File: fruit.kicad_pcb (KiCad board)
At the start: 2 copper layers, 161.6 x 100 mm, 3 parts

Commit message: respin
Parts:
- removed MK2 (x2): Mounting_Hole_PAD, Mounting_Holes:MountingHole_2.7mm
- removed REF**: BUS_PCIexpress_x4, Connector_PCIe_MyOwn:BUS_PCIexpress_x4_Salmonberry_reduced_shoulders
- added C1: 10uF, Capacitor_SMD:C_0402_1005Metric, F.Cu at (548.5, 31.0)
- added C10: 10uF, Capacitor_SMD:C_0402_1005Metric, F.Cu at (475.4, 112.2)
- added C11: 0.1uF, Capacitor_SMD:C_0402_1005Metric, F.Cu at (484.5, 102.6)
- added C12: 1uF, Capacitor_SMD:C_0402_1005Metric, F.Cu at (335.8, 127.8)
- added C13: 1uF, Capacitor_SMD:C_0402_1005Metric, F.Cu at (347.8, 118.3)
- added C14: 0.1uF, Capacitor_SMD:C_0402_1005Metric, F.Cu at (344.9, 120.2)
- added C15: 1uF, Capacitor_SMD:C_0402_1005Metric, F.Cu at (335.8, 129.8)
- added C16: 470pF, Capacitor_SMD:C_0402_1005Metric, F.Cu at (347.7, 120.2)
- added C17: 470pF, Capacitor_SMD:C_0402_1005Metric, F.Cu at (338.8, 125.8)
- added C18: 1uF, Capacitor_SMD:C_0402_1005Metric, F.Cu at (329.2, 139.6)
- added C19: 0.1uF, Capacitor_SMD:C_0402_1005Metric, F.Cu at (341.7, 123.8)
- added C2: 0.1uF, Capacitor_SMD:C_0402_1005Metric, F.Cu at (557.6, 21.4)
- added C20: 0.1uF, Capacitor_SMD:C_0805_2012Metric, F.Cu at (513.1, -59.4)
- added C21: 0.1uF, Capacitor_SMD:C_0805_2012Metric, F.Cu at (496.2, -36.9)
- added C22: 0.1uF, Capacitor_SMD:C_0402_1005Metric, F.Cu at (483.8, 41.3)
- added C23: 1uF, Capacitor_SMD:C_0402_1005Metric, F.Cu at (489.4, 35.3)
- added C24: 0.1uF, Capacitor_SMD:C_0402_1005Metric, F.Cu at (478.3, 46.9)
- added C25: 0.1uF, Capacitor_SMD:C_0402_1005Metric, F.Cu at (496.7, 28.6)
- added C26: 10uF, Capacitor_SMD:C_0805_2012Metric, F.Cu at (495.8, 21.9)
- added C27: 100uF, Capacitor_SMD:C_1210_3225Metric, F.Cu at (490.7, 22.5)
- added C28: 10uF, Capacitor_SMD:C_0805_2012Metric, F.Cu at (476.2, 41.8)
- added C29: 10uF, Capacitor_SMD:C_0805_2012Metric, F.Cu at (490.1, 26.1)
- added C3: 10uF, Capacitor_SMD:C_0402_1005Metric, F.Cu at (335.9, 37.0)
- added C30: 10uF, Capacitor_SMD:C_0805_2012Metric, F.Cu at (490.1, 29.1)
- added C31: 10uF, Capacitor_SMD:C_0805_2012Metric, F.Cu at (494.6, 26.1)
- added C32: 10uF 35V, Capacitor_SMD:C_1206_3216Metric, F.Cu at (575.5, -46.9)
- added C33: 10uF 35V, Capacitor_SMD:C_1206_3216Metric, F.Cu at (569.9, -40.2)
- added C34: 10uF 35V, Capacitor_SMD:C_1206_3216Metric, F.Cu at (569.9, -43.5)
- added C35: 10uF 35V, Capacitor_SMD:C_1206_3216Metric, F.Cu at (569.9, -46.9)
- added C36: 10uF 35V, Capacitor_SMD:C_1206_3216Metric, F.Cu at (587.8, -59.2)
- added C37: 10uF 35V, Capacitor_SMD:C_1206_3216Metric, F.Cu at (578.6, -51.6)
- added C38: 0.1uF, Capacitor_SMD:C_0402_1005Metric, F.Cu at (596.5, -59.9)
- added C39: 0.1uF, Capacitor_SMD:C_0402_1005Metric, F.Cu at (571.4, -35.0)
- added C4: 0.1uF, Capacitor_SMD:C_0402_1005Metric, F.Cu at (329.2, 45.2)
- added C40: DNP, Capacitor_SMD:C_0402_1005Metric, F.Cu at (590.9, -54.5)
- added C41: 1.2nF, Capacitor_SMD:C_0402_1005Metric, F.Cu at (572.5, -37.5)
- added C43: 10uF, Capacitor_SMD:C_0805_2012Metric, F.Cu at (587.2, -56.0)
- added C44: 10uF, Capacitor_SMD:C_0805_2012Metric, F.Cu at (574.9, -43.7)
- added C45: 10uF, Capacitor_SMD:C_0805_2012Metric, F.Cu at (592.8, -59.4)
- added C46: 10uF, Capacitor_SMD:C_0805_2012Metric, F.Cu at (583.6, -51.8)
- added C47: 100uF, Capacitor_Tantalum_SMD_MyOwn:CP_EIA-7343-31_Kemet-D, F.Cu at (572.0, -58.0)
- added C48: 10uF 35V, Capacitor_SMD:C_1206_3216Metric, F.Cu at (421.6, 103.3)
- added C49: 10uF 35V, Capacitor_SMD:C_1206_3216Metric, F.Cu at (409.3, 115.6)
- added C5: 10uF, Capacitor_SMD:C_0402_1005Metric, F.Cu at (360.2, -53.3)
- added C50: 10uF 35V, Capacitor_SMD:C_1206_3216Metric, F.Cu at (412.4, 110.8)
- added C51: 10uF 35V, Capacitor_SMD:C_1206_3216Metric, F.Cu at (403.7, 119.0)
- added C52: 10uF 35V, Capacitor_SMD:C_1206_3216Metric, F.Cu at (403.7, 115.6)
- added C53: 10uF 35V, Capacitor_SMD:C_1206_3216Metric, F.Cu at (403.7, 122.3)
- added C54: 0.1uF, Capacitor_SMD:C_0402_1005Metric, F.Cu at (430.3, 102.6)
- added C55: 0.1uF, Capacitor_SMD:C_0402_1005Metric, F.Cu at (406.4, 125.0)
- added C56: DNP, Capacitor_SMD:C_0402_1005Metric, F.Cu at (405.2, 127.5)
- added C57: 1.2nF, Capacitor_SMD:C_0402_1005Metric, F.Cu at (424.6, 108.0)
- added C59: 10uF, Capacitor_SMD:C_0805_2012Metric, F.Cu at (408.7, 118.8)
- added C6: 0.1uF, Capacitor_SMD:C_0402_1005Metric, F.Cu at (349.2, -42.5)
- added C60: 10uF, Capacitor_SMD:C_0805_2012Metric, F.Cu at (417.4, 110.7)
- added C61: 10uF, Capacitor_SMD:C_0805_2012Metric, F.Cu at (421.0, 106.5)
- added C62: 10uF, Capacitor_SMD:C_0805_2012Metric, F.Cu at (426.6, 103.1)
- added C63: 100uF, Capacitor_Tantalum_SMD_MyOwn:CP_EIA-7343-31_Kemet-D, F.Cu at (405.8, 104.5)
- added C64: 10uF, Capacitor_SMD:C_0402_1005Metric, F.Cu at (41.9, -30.5)
- added C65: 10uF, Capacitor_SMD:C_0402_1005Metric, F.Cu at (124.9, -54.0)
- added C66: 10uF, Capacitor_SMD:C_0402_1005Metric, F.Cu at (47.6, -32.5)
- added C67: 1uF, Capacitor_SMD:C_0402_1005Metric, F.Cu at (36.0, -26.5)
- added C68: 1uF, Capacitor_SMD:C_0402_1005Metric, F.Cu at (33.1, -24.5)
- added C69: 10nF, Capacitor_SMD:C_0402_1005Metric, F.Cu at (39.0, -28.5)
- added C7: 10uF, Capacitor_SMD:C_0805_2012Metric, F.Cu at (445.2, -59.4)
- added C70: 10nF, Capacitor_SMD:C_0402_1005Metric, F.Cu at (33.1, -22.6)
- added C71: 10nF, Capacitor_SMD:C_0402_1005Metric, F.Cu at (36.0, -24.5)
- added C72: 10nF, Capacitor_SMD:C_0402_1005Metric, F.Cu at (36.0, -22.6)
- added C73: 10nF, Capacitor_SMD:C_0402_1005Metric, F.Cu at (44.8, -32.5)
- added C74: 0.1uF, Capacitor_SMD:C_0402_1005Metric, F.Cu at (38.9, -24.6)
- added C8: 10uF, Capacitor_SMD:C_0805_2012Metric, F.Cu at (423.1, -35.6)
- added C9: 10uF, Capacitor_SMD:C_0805_2012Metric, F.Cu at (440.7, -59.4)
- added CM1: ComputeModule4-CM4, Connector_RaspberryPi:Raspberry-Pi-4-Compute-Module_outline, F.Cu at (221.8, -33.1)
- added COOLER1: 53-61mm_NorthBridge_45deg_arms, Mechanical_CoolingBlock:53-61mm_NorthBridge_45deg_arms, F.Cu at (254.9, 103.0)
- added D1: LED Red, LED_SMD_LiteOn:LED_0603_1608Metric_red, F.Cu at (353.9, -53.4)
- added D2: LED Green, LED_SMD_LiteOn:LED_0603_1608Metric_green, F.Cu at (349.8, -50.8)
- added D3: LED Yellow, LED_SMD_LiteOn:LED_0603_1608Metric_yellow, F.Cu at (356.5, -57.0)
- added D4: LED Green, LED_SMD_LiteOn:LED_0603_1608Metric_green, F.Cu at (360.5, -59.6)
- added D5: LED Orange, LED_SMD_LiteOn:LED_0603_1608Metric_orange, F.Cu at (349.8, -53.4)
- added D6: LED Blue, LED_SMD_LiteOn:LED_0603_1608Metric_blue, F.Cu at (356.5, -59.6)
- added D7: LED Green, LED_SMD_LiteOn:LED_0603_1608Metric_green, F.Cu at (476.0, 44.6)
- added D8: LED Green, LED_SMD_LiteOn:LED_0603_1608Metric_green, F.Cu at (569.1, -37.3)
- added D9: LED Green, LED_SMD_LiteOn:LED_0603_1608Metric_green, F.Cu at (402.9, 125.2)
- added FID1: Fiducial, Fiducial:Fiducial_1mm_Mask2mm, F.Cu at (306.1, -59.1)
- added FID2: Fiducial, Fiducial:Fiducial_1mm_Mask2mm, F.Cu at (292.2, -52.1)
- added FID3: Fiducial, Fiducial:Fiducial_1mm_Mask2mm, F.Cu at (221.1, 30.6)
- added H1: MountingHole, MountingHole:MountingHole_2.7mm_M2.5, F.Cu at (3.57, 5.55)
- added H2: MountingHole, MountingHole:MountingHole_2.7mm_M2.5, F.Cu at (3.57, 94.5)
- added J1: PCB_Edge_PCI_Express_x4_Salmonberry, Connector_PCIe_MyOwn:BUS_PCIexpress_x4_Salmonberry_reduced_shoulders, B.Cu at (163.6, 33.5)
- added J2: 2086581051, Connector_HDMI_Molex:2086581051, F.Cu at (429.7, -52.4)
- added J3: TSM-102-01-L-SV, Connector_Header_Samtec:SAMTEC_TSM-102-01-L-SV, F.Cu at (331.1, 121.2)
- added J4: TSM-102-01-L-SV, Connector_Header_Samtec:SAMTEC_TSM-102-01-L-SV, F.Cu at (331.1, 129.1)
- added J5: MEM2067-02-180-00-A_REVB, Connector_SD_GCT:GCT_MEM2067-02-180-00-A_REVB, F.Cu at (502.4, -52.9)
- added J6: USB4110-GF-A, Connector_USB_GCT:USB4110-GF-A, F.Cu at (480.9, 23.3)
- added J7: USB4110-GF-A, Connector_USB_GCT:USB4110-GF-A, F.Cu at (480.9, 33.3)
- added J8: 1-2199119-6, Connector_M.2_TE:1-2199119-6_2280_standoff_nooutline, F.Cu at (115.0, -45.0)
- added L1: SRN6045TA-3R3Y, Inductor_SMD:L_Bourns_SRN6045TA, F.Cu at (580.9, -57.1)
- added L2: SRN6045TA-3R3Y, Inductor_SMD:L_Bourns_SRN6045TA, F.Cu at (414.7, 105.4)
- added R1: 5.1k, Resistor_SMD:R_0402_1005Metric, F.Cu at (329.2, 43.3)
- added R10: 1k, Resistor_SMD:R_0402_1005Metric, F.Cu at (357.3, -54.7)
- added R11: 1k, Resistor_SMD:R_0402_1005Metric, F.Cu at (355.0, -49.0)
- added R12: 1k, Resistor_SMD:R_0402_1005Metric, F.Cu at (349.2, -46.5)
- added R13: 1k, Resistor_SMD:R_0402_1005Metric, F.Cu at (353.3, -51.0)
- added R14: 1k, Resistor_SMD:R_0402_1005Metric, F.Cu at (364.0, -59.9)
- added R15: 1k, Resistor_SMD:R_0402_1005Metric, F.Cu at (356.2, -51.0)
- added R16: 10k, Resistor_SMD:R_0402_1005Metric, F.Cu at (422.3, -33.1)
- added R17: 15k 1%, Resistor_SMD:R_0402_1005Metric, F.Cu at (427.4, -44.6)
- added R18: 1k, Resistor_SMD:R_0402_1005Metric, F.Cu at (329.2, 137.6)
- added R19: 1k, Resistor_SMD:R_0402_1005Metric, F.Cu at (344.9, 118.3)
- added R2: 1k, Resistor_SMD:R_0402_1005Metric, F.Cu at (349.2, -44.5)
- added R20: 1k, Resistor_SMD:R_0402_1005Metric, F.Cu at (335.9, 121.8)
- added R21: 1k, Resistor_SMD:R_0402_1005Metric, F.Cu at (335.9, 123.8)
- added R22: 1k, Resistor_SMD:R_0402_1005Metric, F.Cu at (341.7, 121.9)
- added R23: 1k, Resistor_SMD:R_0402_1005Metric, F.Cu at (338.8, 121.9)
- added R24: 1k, Resistor_SMD:R_0402_1005Metric, F.Cu at (335.9, 125.8)
- added R25: 1k, Resistor_SMD:R_0402_1005Metric, F.Cu at (334.7, 134.1)
- added R26: 1k, Resistor_SMD:R_0402_1005Metric, F.Cu at (338.8, 123.9)
- added R27: 12k 1%, Resistor_SMD:R_0402_1005Metric, F.Cu at (516.8, -59.9)
- added R28: 330R, Resistor_SMD:R_0402_1005Metric, F.Cu at (502.4, 21.4)
- added R29: 5.1k, Resistor_SMD:R_0402_1005Metric, F.Cu at (498.3, 24.4)
- added R3: 1k, Resistor_SMD:R_0402_1005Metric, F.Cu at (359.9, -57.3)
- added R30: 2.2K 1%, Resistor_SMD:R_0402_1005Metric, F.Cu at (498.3, 26.4)
- added R31: 2.2K 1%, Resistor_SMD:R_0402_1005Metric, F.Cu at (475.4, 48.9)
- added R32: 330R, Resistor_SMD:R_0402_1005Metric, F.Cu at (493.8, 28.6)
- added R33: 330R, Resistor_SMD:R_0402_1005Metric, F.Cu at (493.8, 30.6)
- added R34: 5.1k, Resistor_SMD:R_0402_1005Metric, F.Cu at (499.5, 21.4)
- added R35: 10k, Resistor_SMD:R_0402_1005Metric, F.Cu at (479.5, 44.8)
- added R36: 15k 1%, Resistor_SMD:R_0402_1005Metric, F.Cu at (475.4, 46.9)
- added R37: 10R, Resistor_SMD:R_0402_1005Metric, F.Cu at (579.8, -45.9)
- added R38: 12k 1%, Resistor_SMD:R_0402_1005Metric, F.Cu at (587.3, -53.5)
- added R39: 47k 1%, Resistor_SMD:R_0402_1005Metric, F.Cu at (590.9, -56.5)
- added R4: 1k, Resistor_SMD:R_0402_1005Metric, F.Cu at (349.2, -48.5)
- added R40: 15k 1%, Resistor_SMD:R_0402_1005Metric, F.Cu at (568.5, -34.9)
- added R41: 1k, Resistor_SMD:R_0402_1005Metric, F.Cu at (582.9, -49.3)
- added R42: 10R, Resistor_SMD:R_0402_1005Metric, F.Cu at (421.1, 109.0)
- added R43: 20k 1%, Resistor_SMD:R_0402_1005Metric, F.Cu at (416.7, 113.2)
- added R44: 12k 1%, Resistor_SMD:R_0402_1005Metric, F.Cu at (402.3, 127.6)
- added R45: 2.2K 1%, Resistor_SMD:R_0402_1005Metric, F.Cu at (424.7, 106.0)
- added R46: 1k, Resistor_SMD:R_0402_1005Metric, F.Cu at (413.6, 116.6)
- added R47: 50R, Resistor_SMD:R_0402_1005Metric, F.Cu at (122.0, -52.0)
- added R48: 50R, Resistor_SMD:R_0402_1005Metric, F.Cu at (122.0, -53.9)
- added R49: 50R, Resistor_SMD:R_0402_1005Metric, F.Cu at (39.0, -30.5)
- added R5: 5.1k, Resistor_SMD:R_0402_1005Metric, F.Cu at (352.1, -46.5)
- added R50: 50R, Resistor_SMD:R_0402_1005Metric, F.Cu at (36.1, -30.5)
- added R51: 50R, Resistor_SMD:R_0402_1005Metric, F.Cu at (41.9, -32.5)
- added R52: 50R, Resistor_SMD:R_0402_1005Metric, F.Cu at (39.0, -32.5)
- added R53: 50R, Resistor_SMD:R_0402_1005Metric, F.Cu at (36.1, -28.5)
- added R54: 50R, Resistor_SMD:R_0402_1005Metric, F.Cu at (33.2, -32.5)
- added R55: 50R, Resistor_SMD:R_0402_1005Metric, F.Cu at (33.2, -26.5)
- added R56: 50R, Resistor_SMD:R_0402_1005Metric, F.Cu at (36.1, -32.5)
- added R57: 50R, Resistor_SMD:R_0402_1005Metric, F.Cu at (33.2, -28.5)
- added R58: 50R, Resistor_SMD:R_0402_1005Metric, F.Cu at (122.0, -55.9)
- added R59: 50R, Resistor_SMD:R_0402_1005Metric, F.Cu at (125.0, -55.9)
- added R6: 5.1k, Resistor_SMD:R_0402_1005Metric, F.Cu at (362.9, -57.3)
- added R60: 50R, Resistor_SMD:R_0402_1005Metric, F.Cu at (33.2, -30.5)
- added R7: 1k, Resistor_SMD:R_0402_1005Metric, F.Cu at (360.2, -55.3)
- added R8: 1k, Resistor_SMD:R_0402_1005Metric, F.Cu at (352.1, -48.5)
- added R9: 1k, Resistor_SMD:R_0402_1005Metric, F.Cu at (366.9, -59.9)
- added TP1: TestPoint, TestPoint:TestPoint_Pad_D1.0mm, F.Cu at (548.6, 28.5)
- added TP2: TestPoint, TestPoint:TestPoint_Pad_D1.0mm, F.Cu at (475.5, 109.7)
- added TP3: TestPoint, TestPoint:TestPoint_Pad_D1.0mm, F.Cu at (579.9, -48.5)
- added TP4: TestPoint, TestPoint:TestPoint_Pad_D1.0mm, F.Cu at (574.2, -40.7)
- added TP5: TestPoint, TestPoint:TestPoint_Pad_D1.0mm, F.Cu at (413.7, 114.0)
- added TP6: TestPoint, TestPoint:TestPoint_Pad_D1.0mm, F.Cu at (408.0, 121.8)
- added U1: INA260, Sensor_I2C_TI:TSSOP-16_4.4x5mm_P0.65mm_pin1, F.Cu at (551.8, 23.7)
- added U10: LM3525M-H_NPOB, Package_SO_MyOwn:SOIC-8_3.9x4.9mm_P1.27mm, F.Cu at (498.6, -41.7)
- added U11: USB3740B-AI2, Interface_USB_Microchip:Microchip_UQFN-10_1.3x1.8mm_P0.4mm_pin1, F.Cu at (489.8, 32.5)
- added U12: AP22653FDZ-7, Power_Protection_Diodes:Diodes_W-DFN2020-6_A1, F.Cu at (480.6, 42.1)
- added U13: AP64501SP-13, Regulator_Switching_Diodes:SOIC-8-1EP_3.9x4.9mm_P1.27mm_EP2.95x4.9mm_Mask2.71x3.4mm_ThermalVias, F.Cu at (571.5, -51.8)
- added U14: AP64501SP-13, Regulator_Switching_Diodes:SOIC-8-1EP_3.9x4.9mm_P1.27mm_EP2.95x4.9mm_Mask2.71x3.4mm_ThermalVias, F.Cu at (405.3, 110.7)
- added U2: PCA9671BS,118, Interface_I2C_NXP:SOT616-1_HVQFN-24_4x4mm_P0.5mm_EP2.1x2.1mm_NXP, F.Cu at (331.3, 39.2)
- added U3: PCA9671BS,118, Interface_I2C_NXP:SOT616-1_HVQFN-24_4x4mm_P0.5mm_EP2.1x2.1mm_NXP, F.Cu at (351.3, -57.7)
- added U4: AP22653FDZ-7, Power_Protection_Diodes:Diodes_W-DFN2020-6_A1, F.Cu at (440.7, -56.1)
- added U5: TPD8S009DSMR, Power_Protection_TI:DSM15_X_reduced_paste_pin1, F.Cu at (423.6, -41.4)
- added U6: INA260, Sensor_I2C_TI:TSSOP-16_4.4x5mm_P0.65mm_pin1, F.Cu at (478.7, 104.9)
- added U7: MCP9808T-E_MC, Sensor_I2C_Microchip:MCP9808T-E&slash_MC, F.Cu at (330.7, 134.8)
- added U8: ADS7142IRUGR, Analog_ADC_TI:ADS7142IRUGR, F.Cu at (341.9, 119.1)
- added U9: MCP9808T-E_MC, Sensor_I2C_Microchip:MCP9808T-E&slash_MC, F.Cu at (337.4, 119.0)

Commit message: respin
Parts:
- moved C20 571.1 mm to (-47.8, 47.6)
- moved C21 571.1 mm to (-64.8, 70.1)
- moved J5 571.1 mm to (-58.5, 54.1)
- moved R27 571.1 mm to (-44.1, 47.1)
- moved U10 571.1 mm to (-62.3, 65.3)
- moved C32 567.6 mm to (59.3, 189.0)
- moved C33 567.6 mm to (53.7, 195.7)
- moved C34 567.6 mm to (53.7, 192.3)
- moved C35 567.6 mm to (53.7, 189.0)
- moved C36 567.6 mm to (71.6, 176.7)
- moved C37 567.6 mm to (62.4, 184.2)
- moved C38 567.6 mm to (80.3, 176.0)
- moved C39 567.6 mm to (55.2, 200.9)
- moved C40 567.6 mm to (74.6, 181.3)
- moved C43 567.6 mm to (71.0, 179.8)
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
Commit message: respin
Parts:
- moved CM1 0.43 mm to (121.4, 22.6)
- moved COOLER1 0.43 mm to (104.9, 51.1)
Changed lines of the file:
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@@
   )
   (footprint "Connector_RaspberryPi:Raspberry-Pi-4-Compute-Module_outline" (layer "F.Cu")
-    (at 121.05 22.86 180)
+    (at 121.402 22.614 180)
     (descr "Raspberry Pi 4 Compute Module")
     (tags "Raspberry Pi 4 Compute Module")
@@
   )
   (footprint "Mechanical_CoolingBlock:53-61mm_NorthBridge_45deg_arms" (layer "F.Cu")
-    (at 104.55 51.3 90)
+    (at 104.902 51.054 90)
     (descr "53-61mm mounting hole pattern and NorthBridge, 45 deg offset, and arms -- combined.")
     (property "Sheetfile" "fruit.kicad_sch")

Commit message: respin
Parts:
- moved COOLER1 0.80 mm to (104.9, 50.3)
- moved CM1 0.80 mm to (121.4, 21.8)
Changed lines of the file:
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@@
   )
   (footprint "Connector_RaspberryPi:Raspberry-Pi-4-Compute-Module_outline" (layer "F.Cu")
-    (at 121.402 22.614 180)
+    (at 121.402 21.814 180)
     (descr "Raspberry Pi 4 Compute Module")
     (tags "Raspberry Pi 4 Compute Module")
@@
   )
   (footprint "Mechanical_CoolingBlock:53-61mm_NorthBridge_45deg_arms" (layer "F.Cu")
-    (at 104.902 51.054 90)
+    (at 104.902 50.254 90)
     (descr "53-61mm mounting hole pattern and NorthBridge, 45 deg offset, and arms -- combined.")
     (property "Sheetfile" "fruit.kicad_sch")

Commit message: cosmetic
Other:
- board text added: "Place most components on this side"
- board text removed: "Place most components on this side."
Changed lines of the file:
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@@
     (effects (font (size 1 1) (thickness 0.15)))
   )
-  (gr_text "Place most components on this side." (at 80 -10) (layer "Cmts.User")
+  (gr_text "Place most components on this side" (at 80 -10) (layer "Cmts.User")
     (effects (font (size 3 3) (thickness 0.25)))
   )

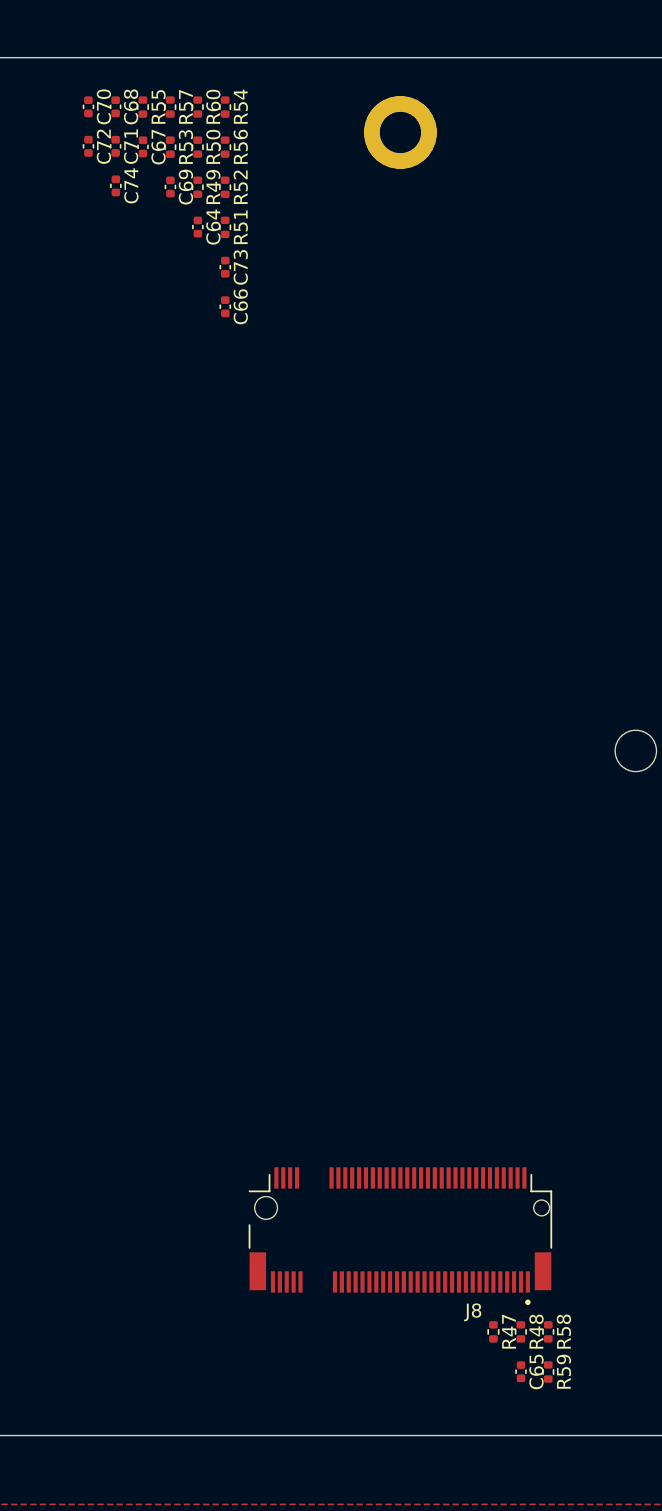
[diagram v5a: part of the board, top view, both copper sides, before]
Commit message: moved m.2 socket around
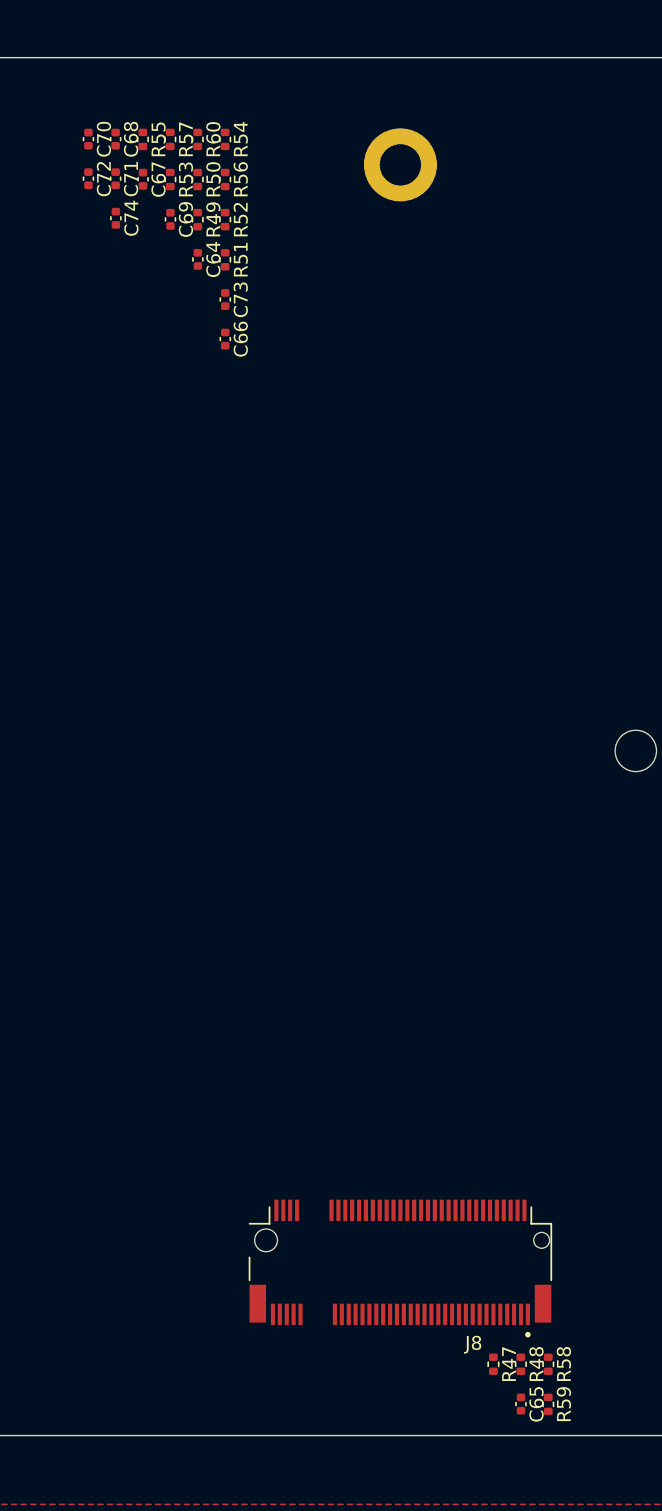
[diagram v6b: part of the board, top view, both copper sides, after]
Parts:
- moved J8 2.35 mm to (50.0, 87.8)
- moved R59 2.35 mm to (60.9, 97.7)
- moved C64 2.35 mm to (35.5, 14.6)
- moved C66 2.35 mm to (37.5, 20.4)
- moved C69 2.35 mm to (33.5, 11.7)
- moved C67 2.35 mm to (31.5, 8.83)
- moved C68 2.35 mm to (29.5, 5.92)
- moved C70 2.35 mm to (27.6, 5.92)
- moved C72 2.35 mm to (27.6, 8.79)
- moved R50 2.35 mm to (35.5, 8.85)
- moved R53 2.35 mm to (33.5, 8.85)
- moved R56 2.35 mm to (37.5, 8.85)
- moved R54 2.35 mm to (37.5, 5.94)
- moved R55 2.35 mm to (31.5, 5.94)
- moved R57 2.35 mm to (33.5, 5.94)
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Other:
- copper layers 2 -> 4

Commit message: locked cm4 & mech footprints
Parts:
- COOLER1: value 53-61mm_NorthBridge_45deg_arms -> 53-61
- J2: value 2086581051 -> CONN_208658-1051_MOL
- J6, J7: value USB4110-GF-A -> GCT_USB4110-GF-A
- U8: value ADS7142IRUGR -> RUG0010A
